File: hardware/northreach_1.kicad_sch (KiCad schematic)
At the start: 16 parts, among them J1 USB_C_Receptacle, J2 Conn_01x03_Pin, J4 Conn_01x03_Pin, SW1 SW_Push, SW2 SW_Push, U1 TPS7A4701xRGW, U2 ESP32-S3-MINI-1U

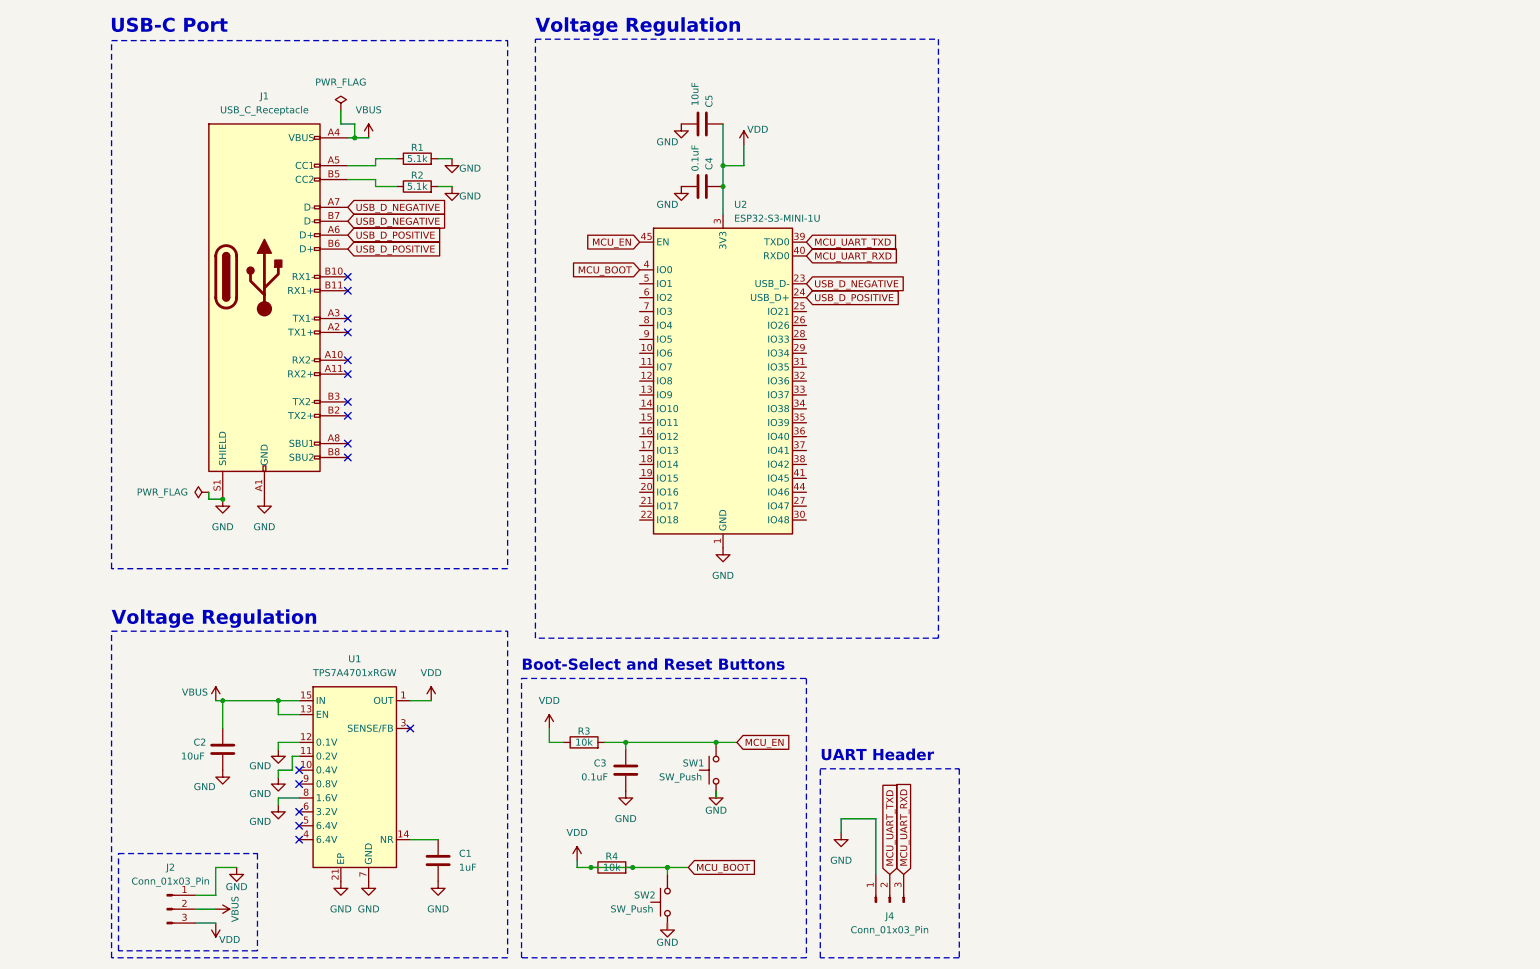
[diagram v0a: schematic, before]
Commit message: schematic: add button array and status led
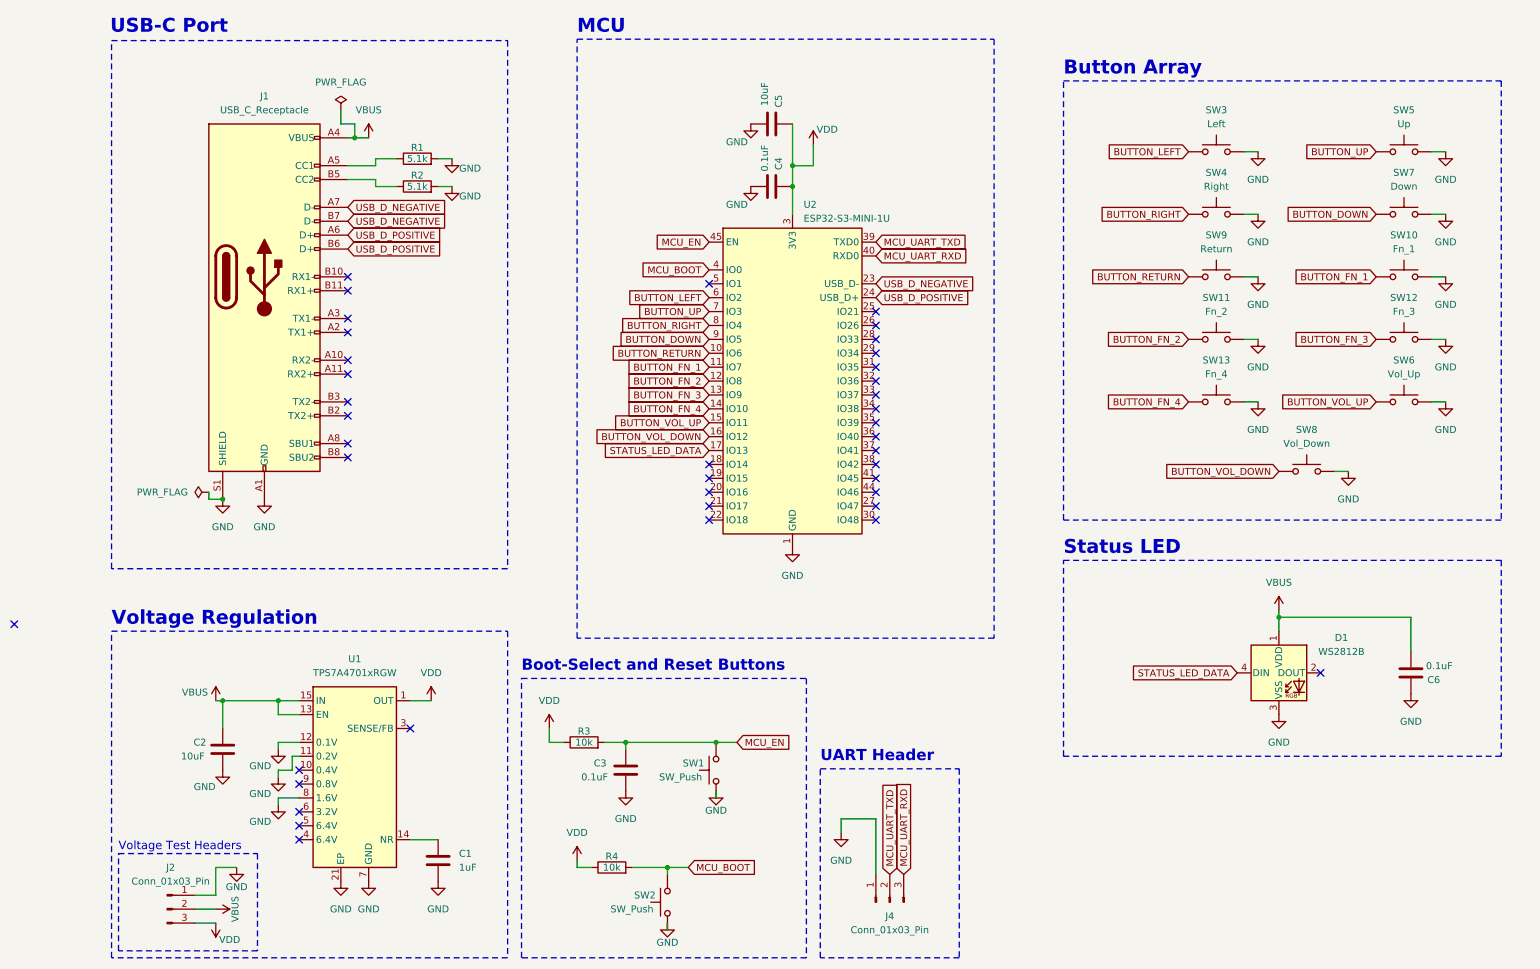
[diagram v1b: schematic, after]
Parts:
- added C6: 0.1uF, Capacitor_SMD:C_0805_2012Metric, symbol Device:C
- added D1: WS2812B, LED_SMD:LED_WS2812B_PLCC4_5.0x5.0mm_P3.2mm, symbol LED:WS2812B
- added SW10: Fn_1, Button_Switch_THT:SW_PUSH_6mm_H5mm, symbol Switch:SW_Push
- added SW11: Fn_2, Button_Switch_THT:SW_PUSH_6mm_H5mm, symbol Switch:SW_Push
- added SW12: Fn_3, Button_Switch_THT:SW_PUSH_6mm_H5mm, symbol Switch:SW_Push
- added SW13: Fn_4, Button_Switch_THT:SW_PUSH_6mm_H5mm, symbol Switch:SW_Push
- added SW3: Left, Button_Switch_THT:SW_PUSH_6mm_H5mm, symbol Switch:SW_Push
- added SW4: Right, Button_Switch_THT:SW_PUSH_6mm_H5mm, symbol Switch:SW_Push
- added SW5: Up, Button_Switch_THT:SW_PUSH_6mm_H5mm, symbol Switch:SW_Push
- added SW6: Vol_Up, Button_Switch_THT:SW_PUSH_6mm_H5mm, symbol Switch:SW_Push
- added SW7: Down, Button_Switch_THT:SW_PUSH_6mm_H5mm, symbol Switch:SW_Push
- added SW8: Vol_Down, Button_Switch_THT:SW_PUSH_6mm_H5mm, symbol Switch:SW_Push
- added SW9: Return, Button_Switch_THT:SW_PUSH_6mm_H5mm, symbol Switch:SW_Push
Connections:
- net GND: now also C6.2, D1.3 (VSS), SW10.2, SW11.2, SW12.2, SW13.2, SW3.2, SW4.2, SW5.2, SW6.2, SW7.2, SW8.2, SW9.2
- net VBUS: now also C6.1, D1.1 (VDD)
- net VDD: no longer R4.2, SW2.2, U2.4 (IO0)
- net BUTTON_RETURN: now reaches U2.10 (IO6)
- net BUTTON_RETURN: now also SW9.1
- net BUTTON_FN_1: now reaches U2.11 (IO7)
- net BUTTON_FN_1: now also SW10.1
- net BUTTON_FN_2: now reaches U2.12 (IO8)
- net BUTTON_FN_2: now also SW11.1
- net BUTTON_FN_3: now reaches U2.13 (IO9)
- net BUTTON_FN_3: now also SW12.1
- net BUTTON_FN_4: now reaches U2.14 (IO10)
- net BUTTON_FN_4: now also SW13.1
- net BUTTON_VOL_UP: now reaches U2.15 (IO11)
- net BUTTON_VOL_UP: now also SW6.1
- net BUTTON_VOL_DOWN: now reaches U2.16 (IO12)
- net BUTTON_VOL_DOWN: now also SW8.1
- net STATUS_LED_DATA: now reaches U2.17 (IO13)
- net STATUS_LED_DATA: now also D1.4 (DIN)
- net BUTTON_LEFT: now reaches U2.6 (IO2)
- net BUTTON_LEFT: now also SW3.1
- net BUTTON_UP: now reaches U2.7 (IO3)
- net BUTTON_UP: now also SW5.1
- net BUTTON_RIGHT: now reaches U2.8 (IO4)
- net BUTTON_RIGHT: now also SW4.1
- net BUTTON_DOWN: now reaches U2.9 (IO5)
- net BUTTON_DOWN: now also SW7.1
- new net MCU_BOOT: R4.2, SW2.2, U2.4 (IO0)
- no-connect marks 16 -> 40
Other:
- note added: "Button Array"
- note added: "MCU"
- note added: "Status LED"
- note added: "Voltage Test Headers"
- moved on the sheet: C4, C5, U2

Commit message: schematic: J4 was missing a footprint
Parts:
- J4: footprint (none) -> Connector_PinHeader_2.54mm:PinHeader_1x03_P2.54mm_Vertical
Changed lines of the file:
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@@
 			)
 		)
-		(property "Footprint" ""
+		(property "Footprint" "Connector_PinHeader_2.54mm:PinHeader_1x03_P2.54mm_Vertical"
 			(at 161.29 180.34 0)
 			(effects

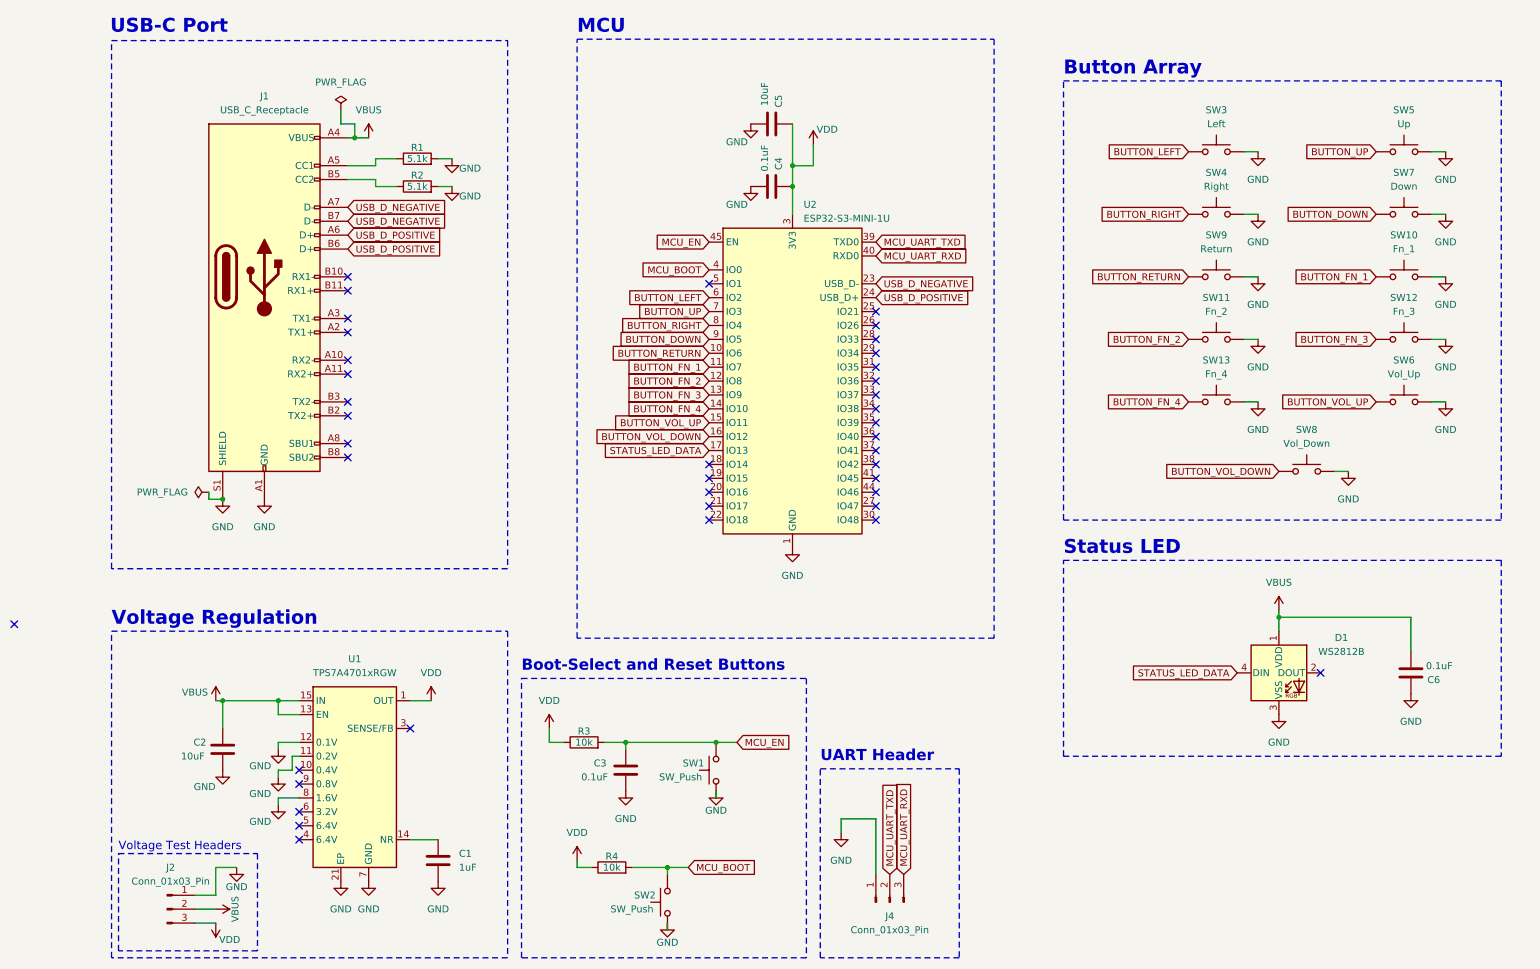
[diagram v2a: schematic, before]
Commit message: schematic: add M2 mounting holes (grounded)
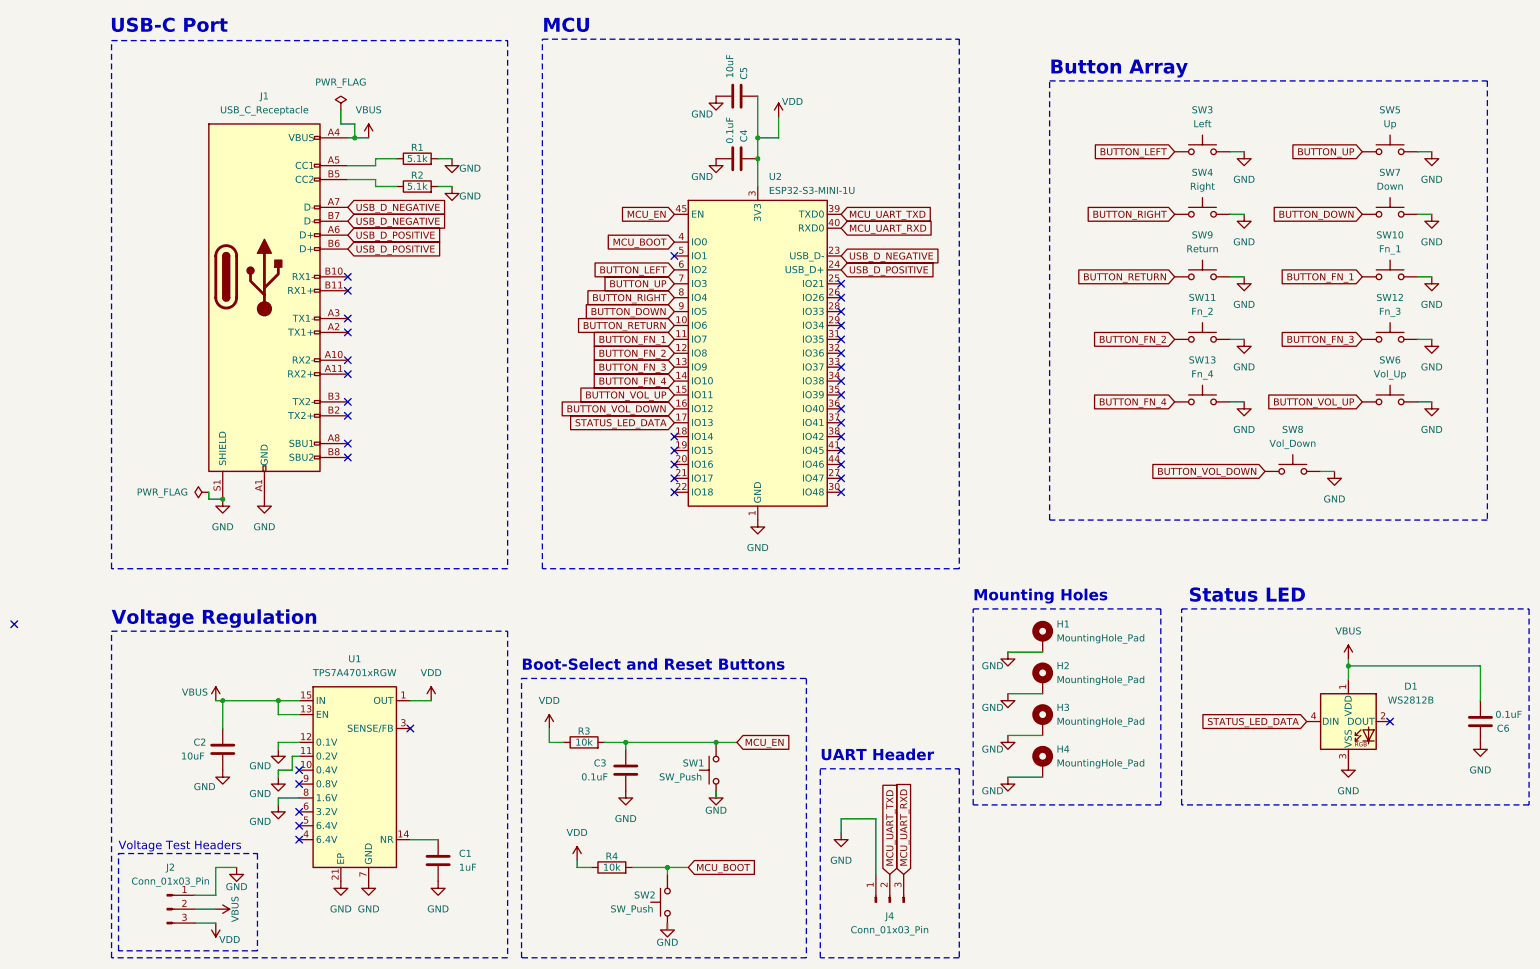
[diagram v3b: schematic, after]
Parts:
- added H1, H2, H3, H4: MountingHole_Pad, MountingHole:MountingHole_2.2mm_M2_Pad, symbol Mechanical:MountingHole_Pad
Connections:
- net GND: now also H1.1, H2.1, H3.1, H4.1
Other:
- note added: "Mounting Holes"
- moved on the sheet: C4, C5, C6, D1, SW10, SW11, SW12, SW13, SW3, SW4, SW5, SW6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
